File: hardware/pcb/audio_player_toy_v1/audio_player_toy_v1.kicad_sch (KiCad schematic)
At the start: 14 parts, among them J1 Conn_02x05_Odd_Even, U1 ISD2360YYI, U2 BH-AAA-B5AA005

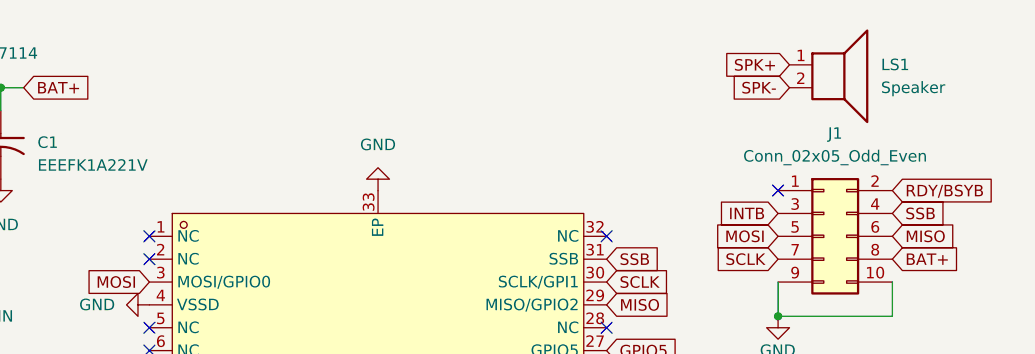
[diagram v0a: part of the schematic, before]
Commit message: feat: add TH speaker capacbility
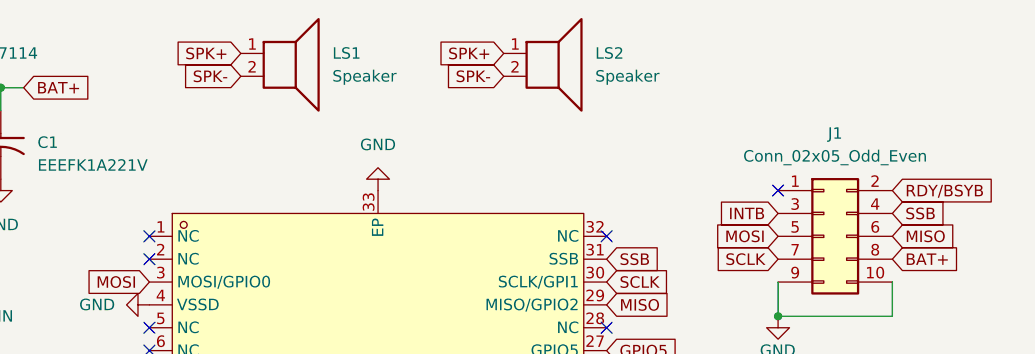
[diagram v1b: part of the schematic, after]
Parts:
- added LS2: Speaker, .pretty:Speaker_TH, symbol Device:Speaker
- LS1: footprint .pretty:Speaker -> .pretty:Speaker_SMD
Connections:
- net SPK+: now also LS2.1
- net SPK-: now also LS2.2
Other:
- moved on the sheet: LS1
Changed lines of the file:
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@@
 	(global_label "SPK-"
 		(shape input)
-		(at 171.45 22.86 180)
+		(at 110.49 21.59 180)
 		(fields_autoplaced yes)
 		(effects
@@
 		)
 		(property "Intersheetrefs" "${INTERSHEET_REFS}"
-			(at 163.1429 22.86 0)
+			(at 102.1829 21.59 0)
 			(effects
 				(font
@@
 	(global_label "SPK+"
 		(shape input)
-		(at 171.45 20.32 180)
+		(at 110.49 19.05 180)
 		(fields_autoplaced yes)
 		(effects
@@
 		)
 		(property "Intersheetrefs" "${INTERSHEET_REFS}"
-			(at 163.1429 20.32 0)
+			(at 102.1829 19.05 0)
 			(effects
 				(font
@@
 		)
 	)
+	(global_label "SPK+"
+		(shape input)
+		(at 139.7 19.05 180)
+		(fields_autoplaced yes)
+		(effects
+			(font
+				(size 1.27 1.27)
+			)
+			(justify right)
+		)
+		(property "Intersheetrefs" "${INTERSHEET_REFS}"
+			(at 131.3929 19.05 0)
+			(effects
+				(font
+					(size 1.27 1.27)
+				)
+				(justify right)
+				(hide yes)
+			)
+		)
+	)
 	(global_label "BAT+"
 		(shape input)
@@
 				)
 				(justify left)
+				(hide yes)
+			)
+		)
+	)
+	(global_label "SPK-"
+		(shape input)
+		(at 139.7 21.59 180)
+		(fields_autoplaced yes)
+		(effects
+			(font
+				(size 1.27 1.27)
+			)
+			(justify right)
+		)
+		(property "Intersheetrefs" "${INTERSHEET_REFS}"
+			(at 131.3929 21.59 0)
+			(effects
+				(font
+					(size 1.27 1.27)
+				)
+				(justify right)
 				(hide yes)
 			)
@@
 	(symbol
 		(lib_id "Device:Speaker")
-		(at 176.53 20.32 0)
+		(at 115.57 19.05 0)
 		(unit 1)
 		(exclude_from_sim no)
@@
 		(fields_autoplaced yes)
 		(property "Reference" "LS1"
-			(at 181.61 20.3199 0)
+			(at 120.65 19.0499 0)
 			(effects
 				(font
@@
 		)
 		(property "Value" "Speaker"
-			(at 181.61 22.8599 0)
+			(at 120.65 21.5899 0)
 			(effects
 				(font
@@
 			)
 		)
-		(property "Footprint" ".pretty:Speaker"
-			(at 176.53 25.4 0)
+		(property "Footprint" ".pretty:Speaker_SMD"
+			(at 115.57 24.13 0)
 			(effects
 				(font
@@
 		)
 		(property "Datasheet" "~"
-			(at 176.276 21.59 0)
+			(at 115.316 20.32 0)
 			(effects
 				(font
@@
 		)
 		(property "Description" "Speaker"
-			(at 176.53 20.32 0)
+			(at 115.57 19.05 0)
 			(effects
 				(font
@@
 					(unit 1)
 				)
+			)
+		)
+	)
+	(symbol
+		(lib_id "Device:Speaker")
+		(at 144.78 19.05 0)
+		(unit 1)
+		(exclude_from_sim no)
+		(in_bom yes)
+		(on_board yes)
+		(dnp no)
+		(fields_autoplaced yes)
+		(property "Reference" "LS2"
+			(at 149.86 19.0499 0)
+			(effects
+				(font
+					(size 1.27 1.27)
+				)
+				(justify left)
+			)
+		)
+		(property "Value" "Speaker"
+			(at 149.86 21.5899 0)
+			(effects
+				(font
+					(size 1.27 1.27)
+				)
+				(justify left)
+			)
+		)
+		(property "Footprint" ".pretty:Speaker_TH"
+			(at 144.78 24.13 0)
+			(effects
+				(font
+					(size 1.27 1.27)
+				)
+				(hide yes)
+			)
+		)
+		(property "Datasheet" "~"
+			(at 144.526 20.32 0)
+			(effects
+				(font
+					(size 1.27 1.27)
+				)
+				(hide yes)
+			)
+		)
+		(property "Description" "Speaker"
+			(at 144.78 19.05 0)
+			(effects
+				(font
+					(size 1.27 1.27)
+				)
+				(hide yes)
+			)
+		)
+		(pin "1"
+		)
+		(pin "2"
+		)
+		(instances
+			(project "audio_player_toy_v1"
+				(path "/cc88cd3f-6086-49ef-b4e9-3dfe485946b1"
+					(reference "LS2")
+					(unit 1)
+				)

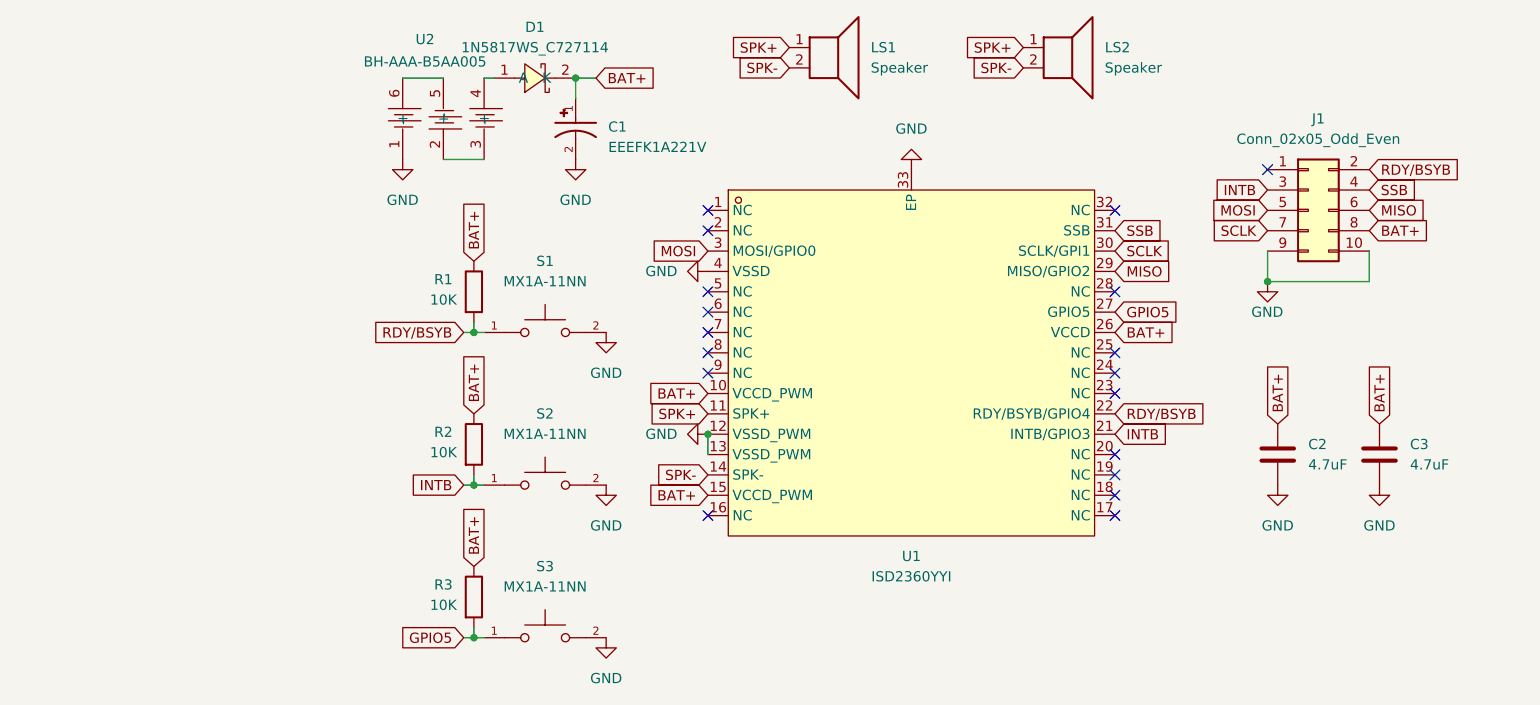
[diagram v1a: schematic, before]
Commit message: chore: resize the pcb
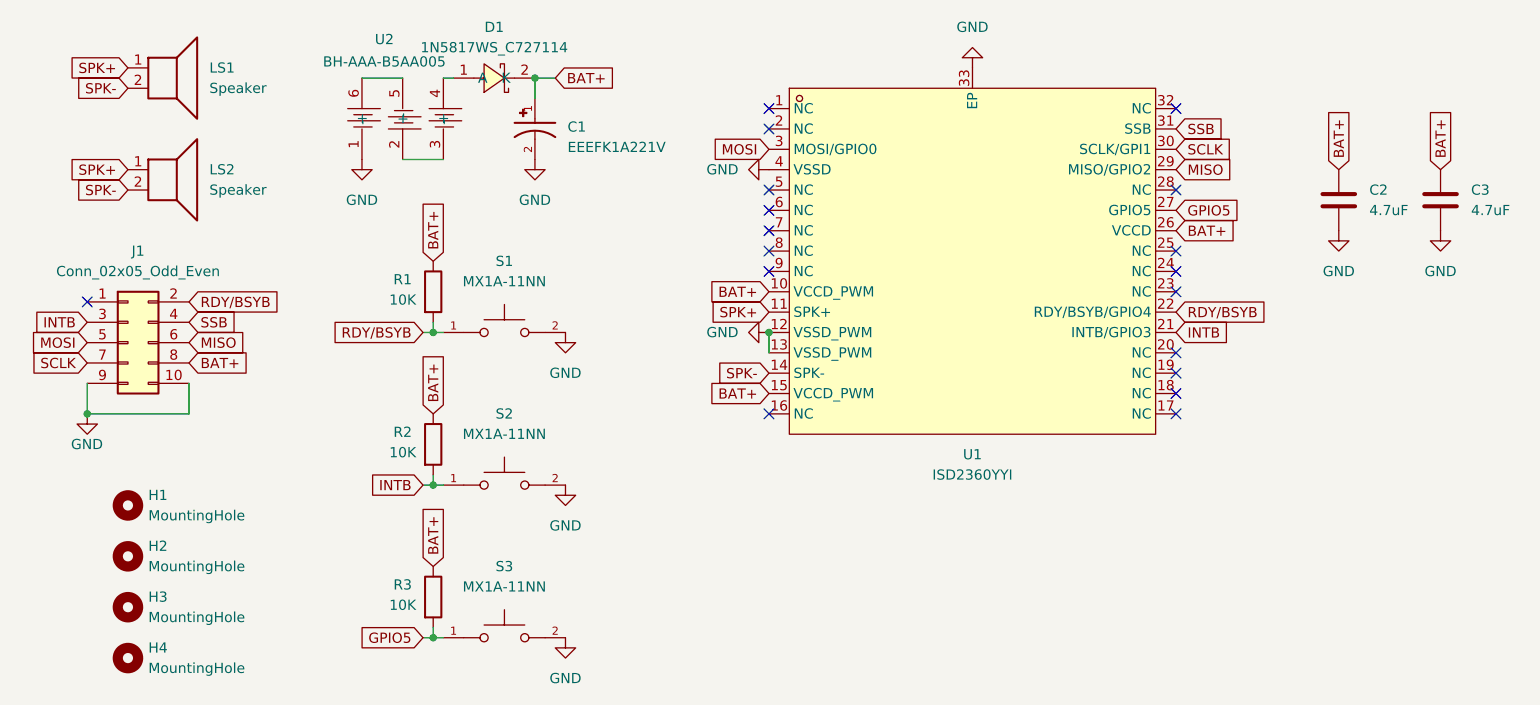
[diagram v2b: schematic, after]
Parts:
- added H1, H2, H3, H4: MountingHole, MountingHole:MountingHole_3.2mm_M3, symbol Mechanical:MountingHole
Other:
- moved on the sheet: C1, C2, C3, D1, J1, LS1, LS2, R1, R2, R3, S1, S2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

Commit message: feat: finish routing pcb
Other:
- moved on the sheet: C1
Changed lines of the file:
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@@
 	(symbol
 		(lib_id "EEEFK1A221V:EEEFK1A221V")
-		(at 78.74 27.94 270)
+		(at 78.74 27.94 90)
+		(mirror x)
 		(unit 1)
 		(exclude_from_sim no)
@@
 		(dnp no)
 		(property "Reference" "C1"
-			(at 82.804 28.956 90)
+			(at 74.676 28.956 90)
 			(effects
 				(font
@@
 		)
 		(property "Value" "EEEFK1A221V"
-			(at 82.804 31.496 90)
+			(at 74.676 31.496 90)
 			(effects
 				(font

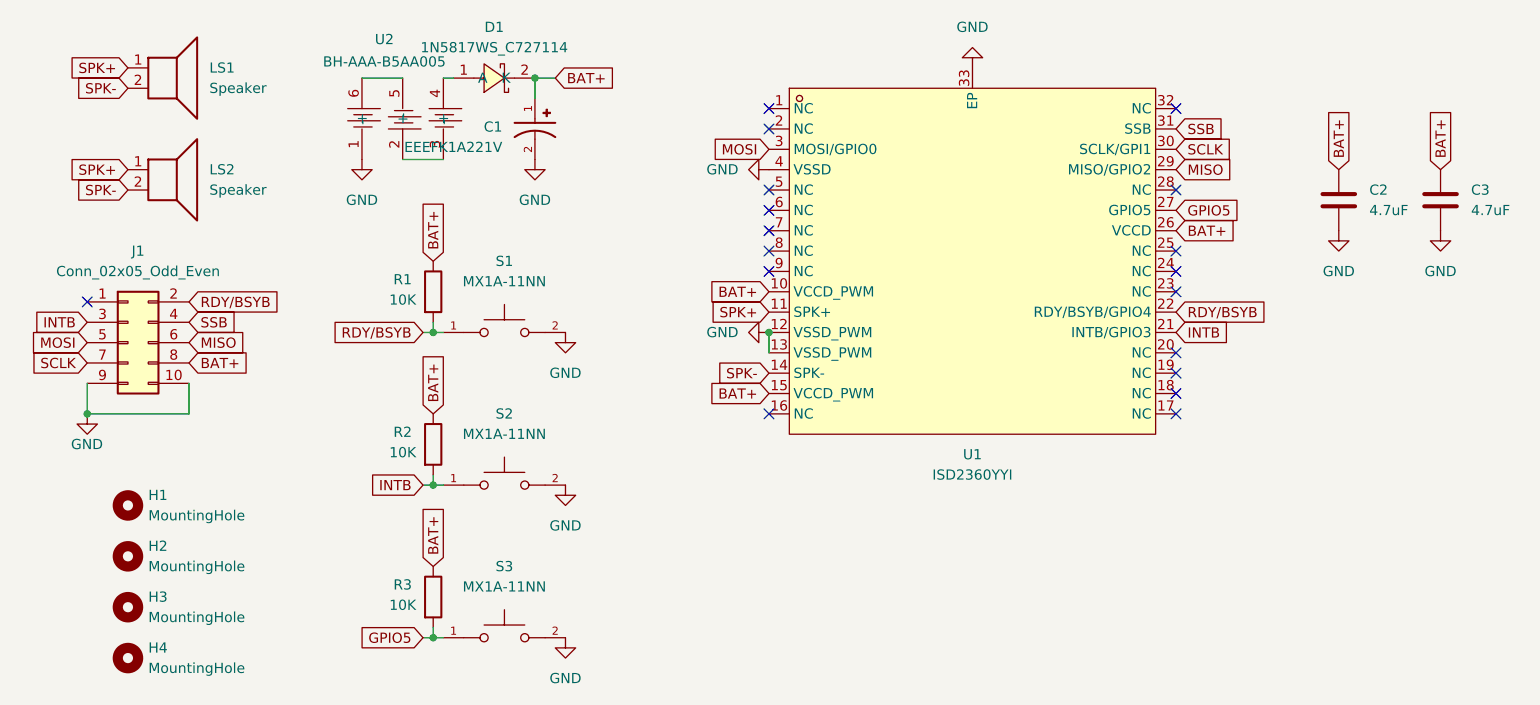
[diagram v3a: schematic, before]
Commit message: chore: change combination of decoupling caps in both versions
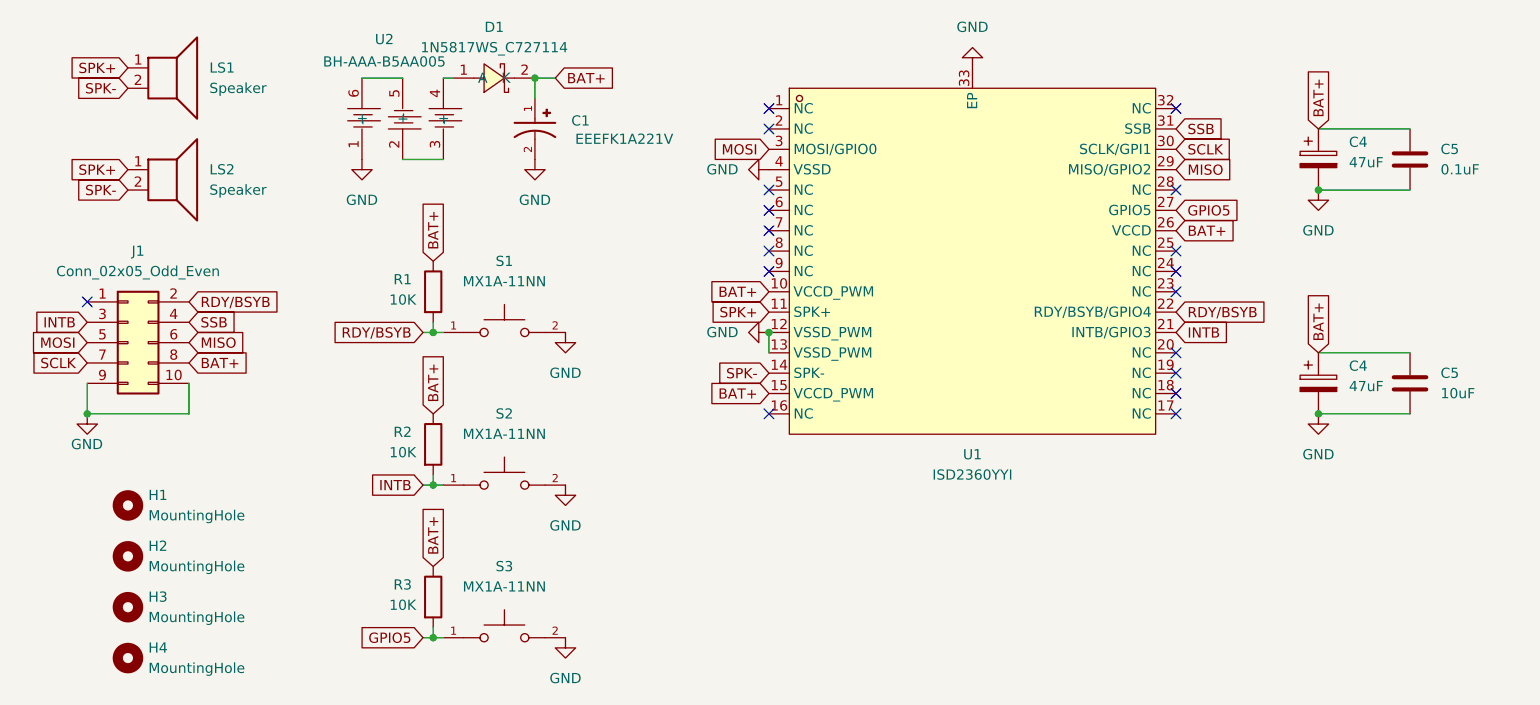
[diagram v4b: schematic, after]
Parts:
- removed C2, C3: 4.7uF, Capacitor_SMD:C_0603_1608Metric, symbol Device:C
- added C4 (x2): 47uF, symbol Device:C_Polarized
- added C5: 10uF, Resistor_SMD:R_0603_1608Metric, symbol Device:C
- added C5: 0.1uF, Resistor_SMD:R_0603_1608Metric, symbol Device:C
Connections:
- net BAT+: now also C4.1, C4.1, C5.1, C5.1
- net GND: now also C4.2, C4.2, C5.2, C5.2

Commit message: chore: complete finding all footprints, ready to routing, both version
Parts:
- C1: Component (none) -> EEEFK1A221V; Manufactor (none) -> PANASONIC
- C2, C3: renamed from C4; footprint (none) -> .pretty:CASE-A_3216; Component (none) -> TLJA476M010R0600; Detail (none) -> +-20%, 10V, 600mΩ; Manufactor (none) -> KYOCERA AVX
- renumbered C5 to C4, U2 to U1, U1 to U2

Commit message: feat: complete sch and pcb of v1
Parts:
- removed C1: EEEFK1A221V, .pretty:CAP_EEEFK1A221V, symbol EEEFK1A221V:EEEFK1A221V
- removed H1, H2, H3, H4: MountingHole, MountingHole:MountingHole_3.2mm_M3, symbol Mechanical:MountingHole
- removed R1, R2: 10K, Resistor_SMD:R_0603_1608Metric, symbol Device:R
- removed S1, S2: MX1A-11NN, .pretty:SW_MX1A-11NN, symbol MX1A-11NN:MX1A-11NN
- added C1: TAJA226M010RNJ, .pretty:CAPMP3216X180N, symbol TAJA226M010RNJ:TAJA226M010RNJ
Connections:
- net BAT+: now also C1.1
- net GND: now also C1.2
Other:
- moved on the sheet: R3, S3
